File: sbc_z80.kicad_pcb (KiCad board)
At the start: 4 copper layers, 101.6 x 50.8 mm, 41 parts, among them J1 RC80 Bus, J2 UPDI TTL, J3 Conn_02x12_Odd_Even, J4 Conn_01x06, J5 Conn_01x06, U1 CPU - Z84C0010AEG, U10 74HC3G34DP,125, U11 AZ1117CH-3.3TRG1, U2 Si5351A-B-GT, U3 SRAM - IS62C5128BL-45TLI, U4 ROM - GLS29EE512, U5 ATtiny1614-SS, U6 SIO/3 - Z84C4310AEG, U7 CPLD - EPM7032STC44, U8 CTC - Z84C3010AEG, U9 PIO - Z84C2010AEG, Y1 25MHZ 8PF

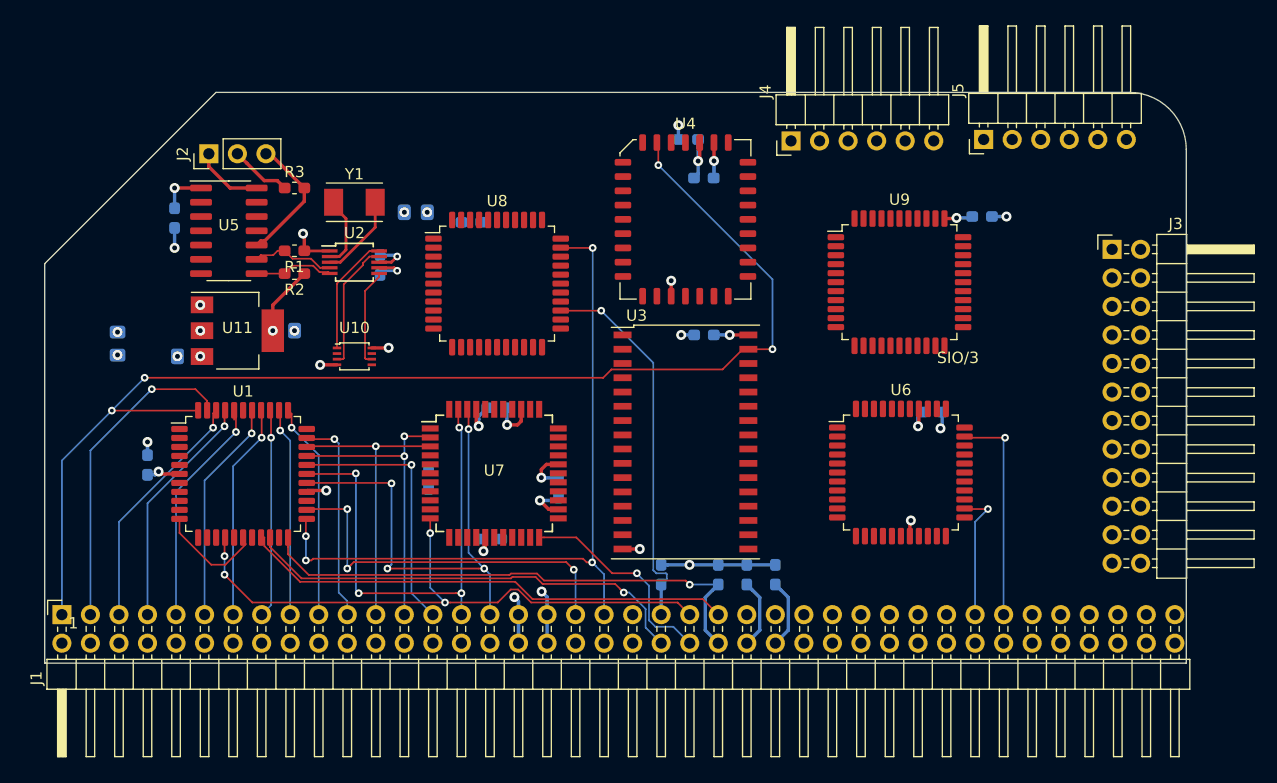
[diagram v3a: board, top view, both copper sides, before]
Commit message: fixed up ce signals
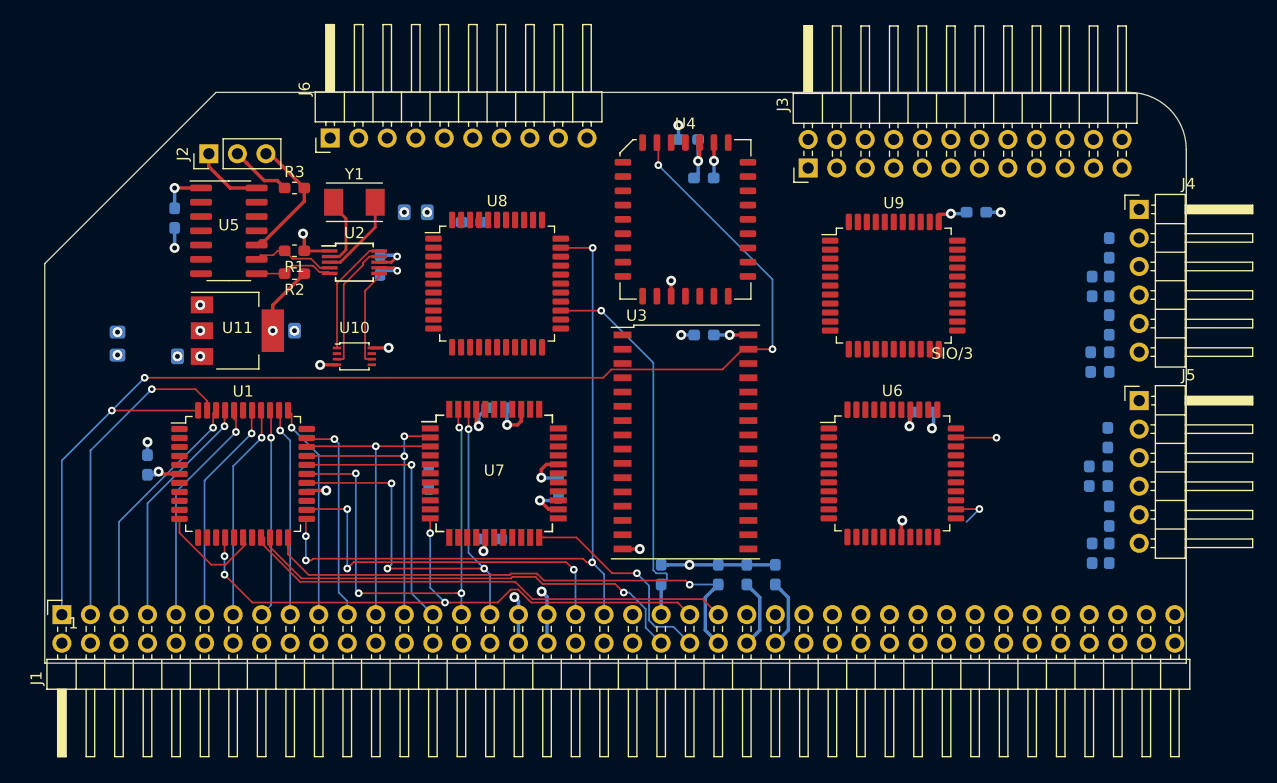
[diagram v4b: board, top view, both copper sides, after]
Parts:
- added J6: Conn_01x10, Connector_PinHeader_2.54mm:PinHeader_1x10_P2.54mm_Horizontal, F.Cu at (100.8, 80.8)
- added R10: 2.2K, Resistor_SMD:R_0603_1608Metric_Pad1.05x0.95mm_HandSolder, B.Cu at (170.2, 90.6)
- added R11: 2.2K, Resistor_SMD:R_0603_1608Metric_Pad1.05x0.95mm_HandSolder, B.Cu at (170.2, 94.0)
- added R12: 2.2K, Resistor_SMD:R_0603_1608Metric_Pad1.05x0.95mm_HandSolder, B.Cu at (170.2, 97.4)
- added R13: 2.2K, Resistor_SMD:R_0603_1608Metric_Pad1.05x0.95mm_HandSolder, B.Cu at (168.5, 100.7)
- added R14: 100K, Resistor_SMD:R_0603_1608Metric_Pad1.05x0.95mm_HandSolder, B.Cu at (170.2, 100.7)
- added R15: 100K, Resistor_SMD:R_0603_1608Metric_Pad1.05x0.95mm_HandSolder, B.Cu at (170.1, 110.9)
- added R16: 2.2K, Resistor_SMD:R_0603_1608Metric_Pad1.05x0.95mm_HandSolder, B.Cu at (170.1, 107.4)
- added R17: 2.2K, Resistor_SMD:R_0603_1608Metric_Pad1.05x0.95mm_HandSolder, B.Cu at (168.4, 110.9)
- added R18: 2.2K, Resistor_SMD:R_0603_1608Metric_Pad1.05x0.95mm_HandSolder, B.Cu at (170.2, 114.4)
- added R19: 2.2K, Resistor_SMD:R_0603_1608Metric_Pad1.05x0.95mm_HandSolder, B.Cu at (168.7, 117.7)
- added R20: 100K, Resistor_SMD:R_0603_1608Metric_Pad1.05x0.95mm_HandSolder, B.Cu at (170.2, 117.7)
- added R9: 100K, Resistor_SMD:R_0603_1608Metric_Pad1.05x0.95mm_HandSolder, B.Cu at (168.7, 94.0)
- moved J4 31.6 mm to (172.8, 87.1), turned to 0 degrees
- moved J3 28.0 mm to (143.4, 83.4), turned to 90 degrees
- moved J5 27.1 mm to (172.8, 104.1), turned to 0 degrees
- moved U6 0.77 mm to (150.9, 110.6)
- moved C11 0.76 mm to (153.7, 105.2)
- moved C12 0.64 mm to (158.4, 87.4)
- moved U9 0.59 mm to (151.0, 93.9)
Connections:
- J1 pad 35: (no net) -> /TXA
- J1 pad 36: (no net) -> /RXA
- J1 pad 54: /A18 -> (no net)
- J1 pad 55: /A17 -> (no net)
- J1 pad 56: /A16 -> (no net)
- J1 pad 60: (no net) -> /~PAGE
- J1 pad 75: (no net) -> /TXB
- J1 pad 76: (no net) -> /RXB
- J4 pad 1: (no net) -> GND
- J4 pad 2: (no net) -> Net-(J4-Pad2)
- J4 pad 4: (no net) -> Net-(J4-Pad4)
- J4 pad 5: (no net) -> Net-(J4-Pad5)
- J4 pad 6: (no net) -> Net-(J4-Pad6)
- J5 pad 1: (no net) -> GND
- J5 pad 2: (no net) -> Net-(J5-Pad2)
- J5 pad 4: (no net) -> Net-(J5-Pad4)
- J5 pad 5: (no net) -> Net-(J5-Pad5)
- J5 pad 6: (no net) -> Net-(J5-Pad6)
- U3 pad 1: /A17 -> GND
- U3 pad 2: /A16 -> /~BANK
- U3 pad 22: /RAM_CE -> /~PAGE
- U3 pad 24: /~RD -> /~MEMRD
- U3 pad 29: /~WR -> /~MEMWR
- U3 pad 30: /A18 -> GND
- U4 pad 22: (no net) -> /PAGE
- U6 pad 11: (no net) -> /TXB
- U6 pad 14: (no net) -> /RXB
- U6 pad 2: (no net) -> /~RTSA
- U6 pad 3: (no net) -> /~CTSA
- U6 pad 4: (no net) -> GND
- U6 pad 41: (no net) -> /RXA
- U6 pad 44: (no net) -> /TXA
- U6 pad 7: (no net) -> GND
- U6 pad 8: (no net) -> /~CTSB
- U6 pad 9: (no net) -> /~RTSB
- U7 pad 10: /~IORQ -> /D0
- U7 pad 11: /~MREQ -> /D7
- U7 pad 12: /~RD -> /~IORQ
- U7 pad 13: /~WR -> /~MREQ
- U7 pad 14: (no net) -> /~RD
- U7 pad 15: (no net) -> /~WR
- U7 pad 21: /~WAIT -> (no net)
- U7 pad 22: /~HALT -> (no net)
- U7 pad 25: (no net) -> /~BANK
- U7 pad 27: (no net) -> /~PAGE
- U7 pad 28: (no net) -> /PAGE
- U7 pad 30: (no net) -> /CTC_CE
- U7 pad 31: (no net) -> /~MEMRD
- U7 pad 33: (no net) -> /~MEMWR
- U7 pad 35: /RAM_CE -> (no net)
- U8 pad 14: (no net) -> /~RD
- U8 pad 21: (no net) -> /~IORQ
- U8 pad 27: (no net) -> /~M1
- U8 pad 31: (no net) -> /CTC_CE
- U8 pad 32: /~RESET -> (no net)
- U8 pad 33: (no net) -> /A0
- U8 pad 35: (no net) -> /A1
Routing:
- net /D7: track 19.5 -> 3.83 mm
- net /D6: track 12.0 -> 3.72 mm

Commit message: reordered resistors
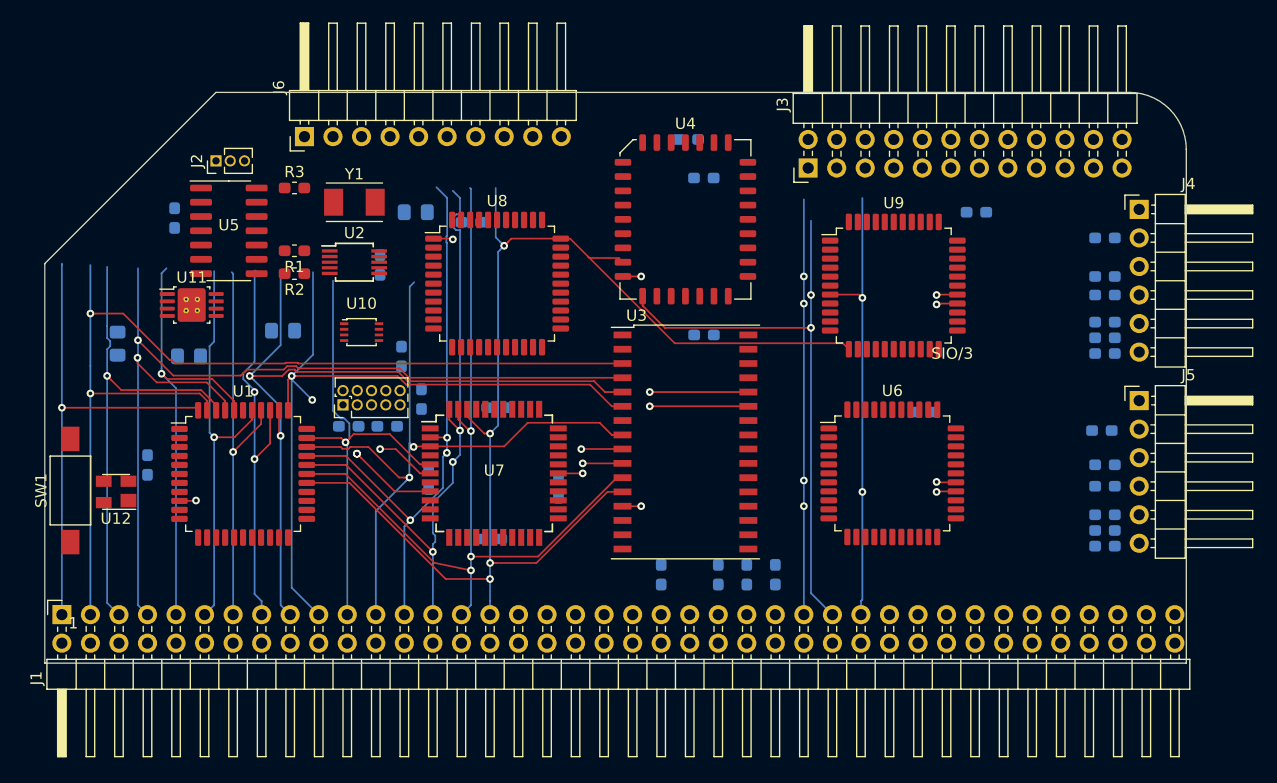
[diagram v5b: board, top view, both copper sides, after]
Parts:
- added J7: AVR-JTAG-10, Connector_PinHeader_1.27mm:PinHeader_2x05_P1.27mm_Vertical, F.Cu at (102.0, 104.5)
- added R21: 1K, Resistor_SMD:R_0603_1608Metric_Pad1.05x0.95mm_HandSolder, B.Cu at (107.2, 100.2)
- added R22: 10K, Resistor_SMD:R_0603_1608Metric_Pad1.05x0.95mm_HandSolder, B.Cu at (105.9, 106.4)
- added R23: 10K, Resistor_SMD:R_0603_1608Metric_Pad1.05x0.95mm_HandSolder, B.Cu at (102.5, 106.4)
- added R24: 10K, Resistor_SMD:R_0603_1608Metric_Pad1.05x0.95mm_HandSolder, B.Cu at (109.0, 104.0)
- added SW1: SW_Push, Button_Switch_SMD:SW_SPST_FSMSM, F.Cu at (77.7, 112.1)
- added U12: MIC811LUY, Package_TO_SOT_SMD:SOT-143, F.Cu at (81.8, 112.3)
- J2: footprint Connector_PinHeader_2.54mm:PinHeader_1x03_P2.54mm_Vertical -> Connector_PinHeader_1.27mm:PinHeader_1x03_P1.27mm_Vertical
- U11: value AZ1117CH-3.3TRG1 -> MIC5356-SGYMME; footprint Package_TO_SOT_SMD:SOT-223-3_TabPin2 -> Package_SO:MSOP-8-1EP_3x3mm_P0.65mm_EP2.5x3mm_Mask1.73x2.36mm_ThermalVias
- moved U11 4.66 mm to (88.5, 95.6)
- moved J6 2.29 mm to (98.6, 80.6)
- moved U10 2.25 mm to (103.6, 98.0)
- moved R14 2.19 mm to (169.8, 98.6), turned to 180 degrees
- moved R20 2.07 mm to (169.8, 115.7), turned to 180 degrees
- moved R17 1.73 mm to (169.8, 109.9), turned to 180 degrees
- moved R13 1.48 mm to (169.8, 99.9), turned to 180 degrees
- moved R9 1.45 mm to (169.8, 93.1), turned to 0 degrees
- moved R19 1.31 mm to (169.8, 117.1), turned to 180 degrees
- moved R10 0.97 mm to (169.8, 89.7), turned to 180 degrees
- moved R15 0.92 mm to (169.8, 111.8), turned to 0 degrees
- moved J2 0.90 mm to (90.7, 82.8)
- moved R11 0.85 mm to (169.8, 94.7), turned to 180 degrees
- moved R16 0.83 mm to (169.5, 106.8), turned to 180 degrees
- moved R12 0.46 mm to (169.8, 97.2), turned to 180 degrees
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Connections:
- U10 pad 2: (no net) -> /CLK_U
- U10 pad 7: (no net) -> /CLK_F
- U11 pad 1: GND -> +5V
- U11 pad 2: +3V3 -> GND
- U11 pad 3: +5V -> (no net)
- U3 pad 1: GND -> /BANK2
- U3 pad 2: /~BANK -> /BANK1
- U3 pad 30: GND -> /BANK3
- U6 pad 12: (no net) -> /CLK_U
- U6 pad 13: (no net) -> /CLK_U
- U6 pad 42: (no net) -> /CLK_U
- U6 pad 43: (no net) -> /CLK_U
- U7 pad 1: (no net) -> /TDI
- U7 pad 18: (no net) -> /~PAGE
- U7 pad 19: (no net) -> /PAGE
- U7 pad 20: (no net) -> /BANK3
- U7 pad 21: (no net) -> /BANK2
- U7 pad 22: (no net) -> /BANK1
- U7 pad 23: (no net) -> /D3
- U7 pad 25: /~BANK -> /D2
- U7 pad 26: (no net) -> /TCK
- U7 pad 27: /~PAGE -> /D1
- U7 pad 28: /PAGE -> /D0
- U7 pad 32: (no net) -> /TDO
- U7 pad 37: (no net) -> /CLK_F
- U7 pad 7: (no net) -> /TMS
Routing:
- net /D0: track 0.00 -> 175.7 mm, vias 0 -> 11
- net /A13: track 21.8 -> 100.5 mm, vias 1 -> 2
- net /A0: track 43.0 -> 114.7 mm
- net /A15: track 111.6 -> 43.5 mm, vias 4 -> 1
- net /A7: track 18.6 -> 85.1 mm, vias 1 -> 4
- net /A12: track 21.2 -> 87.7 mm, vias 1 -> 2
- net /D1: track 0.00 -> 65.8 mm, vias 0 -> 3
- net /~RESET: track 65.4 -> 0.00 mm, vias 4 -> 0
- net /A14: track 28.6 -> 91.9 mm, vias 1 -> 2
- net /A8: track 18.6 -> 81.7 mm, vias 1 -> 3
- net /A6: track 19.3 -> 82.1 mm, vias 1 -> 3
- net /~MREQ: track 55.2 -> 0.00 mm, vias 4 -> 0
- net /A2: track 23.5 -> 71.9 mm, vias 1 -> 4
- net /D2: track 0.00 -> 48.5 mm, vias 0 -> 3
- net /~BUSREQ: track 47.2 -> 0.00 mm, vias 1 -> 0
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- removed copper zone on In1.Cu, net GND

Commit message: changed part layouts
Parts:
- added R25: 10K, Resistor_SMD:R_0603_1608Metric_Pad1.05x0.95mm_HandSolder, B.Cu at (99.8, 83.3)
- added R26: 10K, Resistor_SMD:R_0603_1608Metric_Pad1.05x0.95mm_HandSolder, B.Cu at (105.9, 83.4)
- added R27: 10K, Resistor_SMD:R_0603_1608Metric_Pad1.05x0.95mm_HandSolder, B.Cu at (111.5, 83.7)
- added R28: 10K, Resistor_SMD:R_0603_1608Metric_Pad1.05x0.95mm_HandSolder, B.Cu at (116.6, 83.6)
- J3: value Conn_02x12_Odd_Even -> PIO Header; footprint Connector_PinHeader_2.54mm:PinHeader_2x12_P2.54mm_Horizontal -> Connector_PinHeader_2.54mm:PinHeader_2x13_P2.54mm_Horizontal
- J6: value Conn_01x10 -> CTC Header
- R10, R11, R12, R13, R16, R17, R18, R19: value 2.2K -> 2K2
- U10: value 74HC3G34DP,125 -> 74HC3G04DP,125; footprint Package_SO:VSSOP-8_2.4x2.1mm_P0.5mm -> Package_SO:TSSOP-8_3x3mm_P0.65mm
- U4: value ROM - GLS29EE512 -> GLS29EE010; footprint Package_LCC:PLCC-32_11.4x14.0mm_P1.27mm -> Package_LCC:PLCC-32_SMD-Socket
- moved U1 44.3 mm to (137.4, 113.0)
- moved U8 26.4 mm to (97.6, 113.0)
- moved U3 24.0 mm to (112.5, 94.5)
- moved C4 13.3 mm to (83.4, 97.6), turned to 180 degrees
- moved J7 12.7 mm to (108.6, 115.3), turned to 180 degrees
- moved R23 11.9 mm to (111.2, 114.6), turned to 90 degrees
- moved C12 9.50 mm to (167.9, 87.2)
- moved R22 7.03 mm to (111.2, 111.1), turned to 270 degrees
- moved C11 6.94 mm to (159.7, 108.7)
- moved R2 6.79 mm to (92.7, 97.5)
- moved R3 6.79 mm to (92.7, 89.9)
- moved R1 6.79 mm to (92.7, 95.5)
- moved J2 6.74 mm to (85.9, 87.5)
- moved U5 6.74 mm to (87.0, 93.7)
- moved U6 6.73 mm to (157.2, 113.0)
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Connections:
- C10 pad 1: +5V -> Net-(C10-Pad1)
- C11 pad 1: +5V -> Net-(C10-Pad1)
- C12 pad 1: +5V -> Net-(C10-Pad1)
- C13 pad 1: +5V -> Net-(C10-Pad1)
- C14 pad 1: +5V -> Net-(C10-Pad1)
- C5 pad 1: +5V -> Net-(C10-Pad1)
- C6 pad 1: +5V -> Net-(C10-Pad1)
- C7 pad 1: +5V -> Net-(C10-Pad1)
- C8 pad 1: +5V -> Net-(C10-Pad1)
- C9 pad 1: +5V -> Net-(C10-Pad1)
- J1 pad 54: (no net) -> /A18
- J1 pad 55: (no net) -> /A17
- J1 pad 56: (no net) -> /A16
- J3 pad 1: (no net) -> +5V
- J3 pad 10: (no net) -> /PB2
- J3 pad 11: (no net) -> /PA4
- J3 pad 12: (no net) -> /PB3
- J3 pad 13: (no net) -> /PA5
- J3 pad 14: (no net) -> /PB4
- J3 pad 15: (no net) -> /PA6
- J3 pad 16: (no net) -> /PB5
- J3 pad 17: (no net) -> /PA7
- J3 pad 18: (no net) -> /PB6
- J3 pad 19: (no net) -> /ARDY
- J3 pad 2: (no net) -> GND
- J3 pad 20: (no net) -> /PB7
- J3 pad 21: (no net) -> /~ASTB
- J3 pad 22: (no net) -> /BRDY
- J3 pad 23: (no net) -> GND
- J3 pad 24: (no net) -> /~BSTB
- J3 pad 3: (no net) -> /PA0
- J3 pad 4: (no net) -> GND
- J3 pad 5: (no net) -> /PA1
- J3 pad 6: (no net) -> /PB0
- J3 pad 7: (no net) -> /PA2
- J3 pad 8: (no net) -> /PB1
- J3 pad 9: (no net) -> /PA3
- J6 pad 1: (no net) -> +5V
- J6 pad 10: (no net) -> GND
- J6 pad 2: (no net) -> /CT0
- J6 pad 3: (no net) -> /ZT0
- J6 pad 4: (no net) -> /CT1
- J6 pad 5: (no net) -> /ZT1
- J6 pad 6: (no net) -> /CT2
- J6 pad 7: (no net) -> /ZT2
- J6 pad 8: (no net) -> /CT3
- U3 pad 1: /BANK2 -> /A17
- U3 pad 2: /BANK1 -> /A16
- U3 pad 30: /BANK3 -> /A18
- U4 pad 2: Net-(U4-Pad1) -> /A16
- U7 pad 20: /BANK3 -> /A18
- U7 pad 21: /BANK2 -> /A17
- U7 pad 22: /BANK1 -> /A16
- U8 pad 16: (no net) -> /ZT0
- U8 pad 18: (no net) -> /ZT1
- U8 pad 19: (no net) -> /ZT2
- U8 pad 32: (no net) -> /~RESET
- U8 pad 36: (no net) -> /CT3
- U8 pad 37: (no net) -> /CT2
- U8 pad 40: (no net) -> /CT1
- U8 pad 41: (no net) -> /CT0
- U9 pad 13: (no net) -> /PA7
- U9 pad 14: (no net) -> /PA6
- U9 pad 15: (no net) -> /PA5
- U9 pad 16: (no net) -> /PA4
- U9 pad 19: (no net) -> /PA3
- U9 pad 20: (no net) -> /PA2
- U9 pad 21: (no net) -> /PA1
- U9 pad 22: (no net) -> /PA0
- U9 pad 23: (no net) -> /~ASTB
- U9 pad 24: (no net) -> /~BSTB
- U9 pad 25: (no net) -> /ARDY
- U9 pad 29: (no net) -> /BRDY
- U9 pad 35: (no net) -> /PB0
- U9 pad 36: (no net) -> /PB1
- U9 pad 37: (no net) -> /PB2
- U9 pad 38: (no net) -> /PB3
- U9 pad 40: (no net) -> /PB4
- U9 pad 41: (no net) -> /PB5
- U9 pad 42: (no net) -> /PB6
- U9 pad 43: (no net) -> /PB7
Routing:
- net /D0: track 175.7 -> 0.00 mm, vias 11 -> 0
- net /A0: track 114.7 -> 0.00 mm, vias 4 -> 0
- net /A13: track 100.5 -> 0.00 mm, vias 2 -> 0
- net /A14: track 91.9 -> 0.00 mm, vias 2 -> 0
- net /A12: track 87.7 -> 0.00 mm, vias 2 -> 0
- net /A7: track 85.1 -> 0.00 mm, vias 4 -> 0
- net /A6: track 82.1 -> 0.00 mm, vias 3 -> 0
- net /A8: track 81.7 -> 0.00 mm, vias 3 -> 0
- net /A1: track 75.2 -> 0.00 mm, vias 3 -> 0
- net /A2: track 71.9 -> 0.00 mm, vias 4 -> 0
- net /A3: track 68.9 -> 0.00 mm, vias 4 -> 0
- net /D1: track 65.8 -> 0.00 mm, vias 3 -> 0
- net /A4: track 61.8 -> 0.00 mm, vias 2 -> 0
- net /D2: track 48.5 -> 0.00 mm, vias 3 -> 0
- net /A15: track 43.5 -> 0.00 mm, vias 1 -> 0
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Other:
- board text added: "CTC"
- board text added: "GND"
- board text added: "GPIO"
- board text added: "JTAG"
- board text added: "MAX 7000 CPLD"
- board text added: "PIO"
- board text added: "Port A"
- board text added: "Port B"
- board text added: "RESET"
- board text added: "ROM 128Kx8"
- board text added: "RXD"
- board text added: "SRAM 512Kx8"
- board text added: "TXD"
- board text added: "UPDI"
- board text added: "VCC"
- board text added: "Z80 CPU"
- board text added: "~CTS"
- board text added: "~RTS"

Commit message: cleanup
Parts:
- removed the C1 at (100.3, 94.9)
- removed the C2 at (82.2, 90.8)
- added C15: 0.47uF, Capacitor_SMD:C_0603_1608Metric_Pad1.05x0.95mm_HandSolder, B.Cu at (89.7, 94.5)
- added C16: 0.47uF, Capacitor_SMD:C_0603_1608Metric_Pad1.05x0.95mm_HandSolder, B.Cu at (90.0, 96.6)
- added D1: Red/Green, LED_SMD:LED_2C_0603_1608Metric_Pad1.05x0.95mm_HandSolder, F.Cu at (79.4, 102.9)
- added R29: 680R, Resistor_SMD:R_0603_1608Metric_Pad1.05x0.95mm_HandSolder, B.Cu at (79.4, 101.1)
- added R30: 680R, Resistor_SMD:R_0603_1608Metric_Pad1.05x0.95mm_HandSolder, B.Cu at (79.4, 104.6)
- added SW3: SW_DIP_x08, Button_Switch_SMD:SW_DIP_SPSTx08_Slide_KingTek_DSHP08TJ_W5.25mm_P1.27mm_JPin, F.Cu at (144.9, 109.7)
- R1, R2, R3: moved to B.Cu
- U10: value 74HC3G04DP,125 -> 74HC04; footprint Package_SO:TSSOP-8_3x3mm_P0.65mm -> Package_SO:TSSOP-14_4.4x5mm_P0.65mm
- U11: value MIC5356-SGYMME -> ATtiny1614-SS; footprint Package_SO:MSOP-8-1EP_3x3mm_P0.65mm_EP2.5x3mm_Mask1.73x2.36mm_ThermalVias -> Package_SO:SOIC-14_3.9x8.7mm_P1.27mm
- U2: value Si5351A-B-GT -> TPS7A0533PDBVR; footprint Package_SO:MSOP-10_3x3mm_P0.5mm -> Package_TO_SOT_SMD:SOT-23-5
- U5: value ATtiny1614-SS -> Si5351A-B-GT; footprint Package_SO:SOIC-14_3.9x8.7mm_P1.27mm -> Package_SO:MSOP-10_3x3mm_P0.5mm
- U7: footprint Package_QFP:TQFP-44_10x10mm_P0.8mm -> Package_QFP:TQFP-100_14x14mm_P0.5mm
- moved J7 34.2 mm to (142.5, 119.6), turned to 90 degrees
- moved U1 25.2 mm to (112.1, 113.0)
- moved U7 13.2 mm to (130.6, 111.5)
- moved U5 13.0 mm to (99.8, 95.9)
- moved U11 9.61 mm to (91.6, 93.2), turned to 0 degrees
- moved U2 8.84 mm to (91.4, 101.3), turned to 90 degrees
- moved J2 5.02 mm to (90.6, 85.7)
- moved U4 3.48 mm to (130.6, 90.7)
- moved U8 2.98 mm to (94.6, 113.0)
- moved R1 2.16 mm to (93.7, 93.5), turned to 0 degrees
- moved R2 2.16 mm to (93.7, 95.6), turned to 0 degrees
- moved R3 2.16 mm to (93.7, 88.0), turned to 180 degrees
- moved Y1 1.66 mm to (100.1, 91.7)
- moved U10 1.33 mm to (99.9, 101.3), turned to 180 degrees
- moved U3 0.41 mm to (112.1, 94.5)
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- renumbered C15 to C1, C16 to C2, C4 to C3, C3 to C4
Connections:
- U10 pad 2: /CLK_U -> /CLK_F
- U10 pad 4: GND -> /CLK
- U10 pad 5: /CLK -> Net-(U10-Pad5)
- U10 pad 6: Net-(U10-Pad6) -> /CLK_U
- U10 pad 7: /CLK_F -> GND
- U10 pad 8: +5V -> Net-(D1-Pad4)
- U11 pad 1: +5V -> +3V3
- U11 pad 2: GND -> (no net)
- U11 pad 4: GND -> (no net)
- U11 pad 5: +5V -> (no net)
- U11 pad 8: +3V3 -> Net-(R2-Pad2)
- U11 pad 9: GND -> Net-(R1-Pad2)
- U2 pad 1: +3V3 -> +5V
- U2 pad 2: Net-(U2-Pad2) -> GND
- U2 pad 3: Net-(U2-Pad3) -> +5V
- U2 pad 4: Net-(R1-Pad2) -> (no net)
- U2 pad 5: Net-(R2-Pad2) -> +3V3
- U5 pad 10: /Clocks/RX -> Net-(U10-Pad1)
- U5 pad 2: (no net) -> Net-(U5-Pad2)
- U5 pad 3: (no net) -> Net-(U5-Pad3)
- U5 pad 4: (no net) -> Net-(R1-Pad2)
- U5 pad 5: (no net) -> Net-(R2-Pad2)
- U5 pad 6: (no net) -> Net-(U10-Pad5)
- U5 pad 7: (no net) -> +3V3
- U5 pad 8: Net-(R2-Pad2) -> GND
- U5 pad 9: Net-(R1-Pad2) -> Net-(U10-Pad3)
- Y1 pad 1: Net-(U2-Pad2) -> Net-(U5-Pad2)
- Y1 pad 2: Net-(U2-Pad3) -> Net-(U5-Pad3)
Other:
- board text added: "ROM ENA"
